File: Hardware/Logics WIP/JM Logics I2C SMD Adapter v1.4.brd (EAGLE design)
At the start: 52.4 x 31.2 mm, 30 parts, among them IC1 MEGA328P, J2 2.1MMJACK, X1 16.00MHz

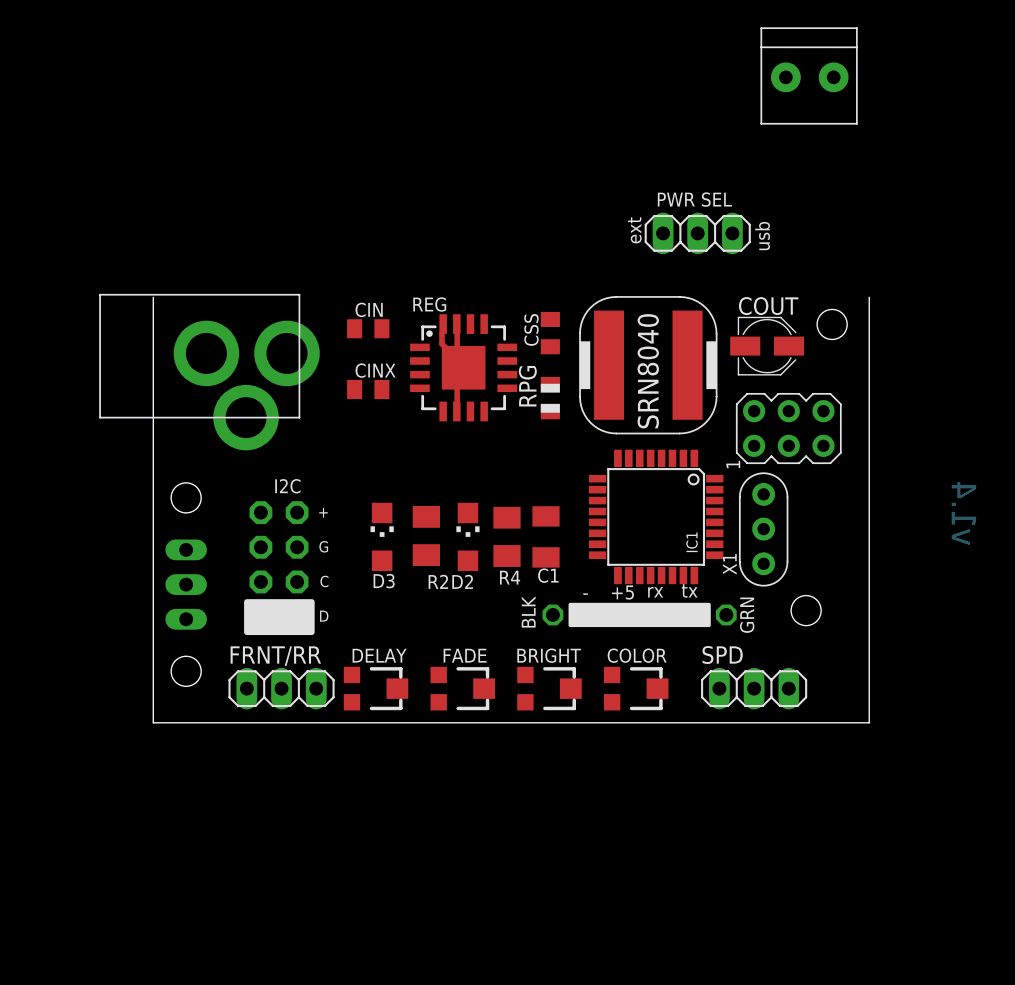
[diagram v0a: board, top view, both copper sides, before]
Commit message: 
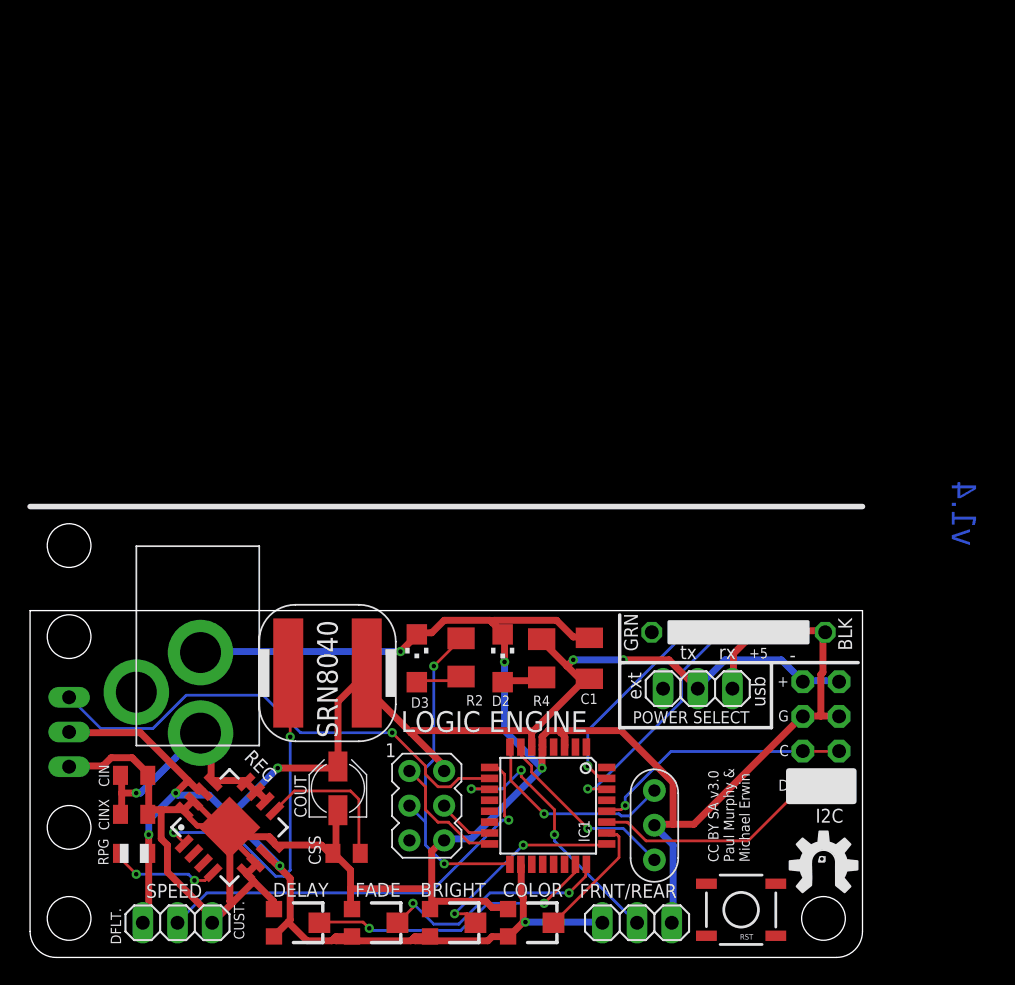
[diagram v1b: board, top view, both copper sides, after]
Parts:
- removed 5VIN: 1X2-3.5MM, adafruit:1X2-3.5MM
- removed FRNT/RR, SPD: (no value), pinhead:1X03
- added FRNT/REAR, SPEED: (no value), pinhead:1X03
- added RST: (no value), SparkFun-Electromechanical:TACTILE_SWITCH_SMD
- X1: value 16.00MHz -> 16MHz
- moved U$2 66.2 mm to (58.0, 6.79), flipped to the top
- moved U$1 59.4 mm to (73.5, 15.2)
- moved RPG 45.2 mm to (7.62, 7.62), turned to 180 degrees
- moved COUT 45.1 mm to (22.5, 12.4), turned to 90 degrees
- moved I2C 41.6 mm to (56.6, 16.4)
- moved I2C1 41.6 mm to (59.2, 16.4)
- moved CSS 40.9 mm to (23.2, 7.62), turned to 180 degrees
- moved ICSP 38.3 mm to (29.1, 11.1), turned to 0 degrees
- moved REG 37.8 mm to (14.6, 9.53), turned to 45 degrees
- moved CIN 36.9 mm to (7.62, 13.3)
- moved CINX 35.5 mm to (7.62, 10.5)
- moved PWR_SEL1 33.3 mm to (48.9, 19.7)
- moved INDUCTOR 32.6 mm to (17.8, 16.8)
- moved X1 23.1 mm to (45.7, 9.68)
- moved IC1 22.6 mm to (37.9, 11.1)
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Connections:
- net +5V: now also FRNT/REAR.1, SPEED.1; no longer FRNT/RR.1, SPD.1
- net DIGITAL5: now also SPEED.2; no longer SPD.2
- net DIGITAL7: now also FRNT/REAR.2; no longer FRNT/RR.2
- net GND: now also FRNT/REAR.3, SPEED.3; no longer FRNT/RR.3, SPD.3
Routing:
- net GND: track 0.00 -> 175.9 mm, vias 0 -> 3
- net +5V: track 0.00 -> 142.6 mm, vias 0 -> 7
- net DIGITAL6: track 0.00 -> 36.1 mm, vias 0 -> 1
- net DIGITAL5: track 0.00 -> 32.2 mm, vias 0 -> 1
- net N$3: track 0.00 -> 25.7 mm, vias 0 -> 2
- net SCK: track 0.00 -> 24.7 mm, vias 0 -> 2
- net ANALOG0: track 0.00 -> 21.3 mm, vias 0 -> 2
- net DIGITAL7: track 0.00 -> 20.3 mm, vias 0 -> 3
- net ANALOG4: track 0.00 -> 19.3 mm
- net ANALOG5: track 0.00 -> 19.2 mm, vias 0 -> 1
- net N$6: track 0.00 -> 19.1 mm, vias 0 -> 1
- net ANALOG1: track 0.00 -> 17.5 mm, vias 0 -> 2
- net RXD: track 0.00 -> 17.2 mm, vias 0 -> 1
- net ANALOG2: track 0.00 -> 15.1 mm, vias 0 -> 2
- net N$2: track 0.00 -> 14.9 mm, vias 0 -> 1
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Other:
- board size 52.4 x 31.2 mm -> 61 x 25.4 mm
- board text added: "CC BY SA v3.0 Paul Murphy & Michael Erwin"
- board text added: "CUST."
- board text added: "DFLT."
- board text added: "LOGIC ENGINE"
- board text added: "POWER SELECT"
- board text removed: "Logic Engine CC v3 BY SA 2013 Paul Murphy & Michael Erwin"
- board text removed: "PWR SEL"
- board text removed: "X1"

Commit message: Need to repackage inductor on Logic Engine to include GND (duh!)
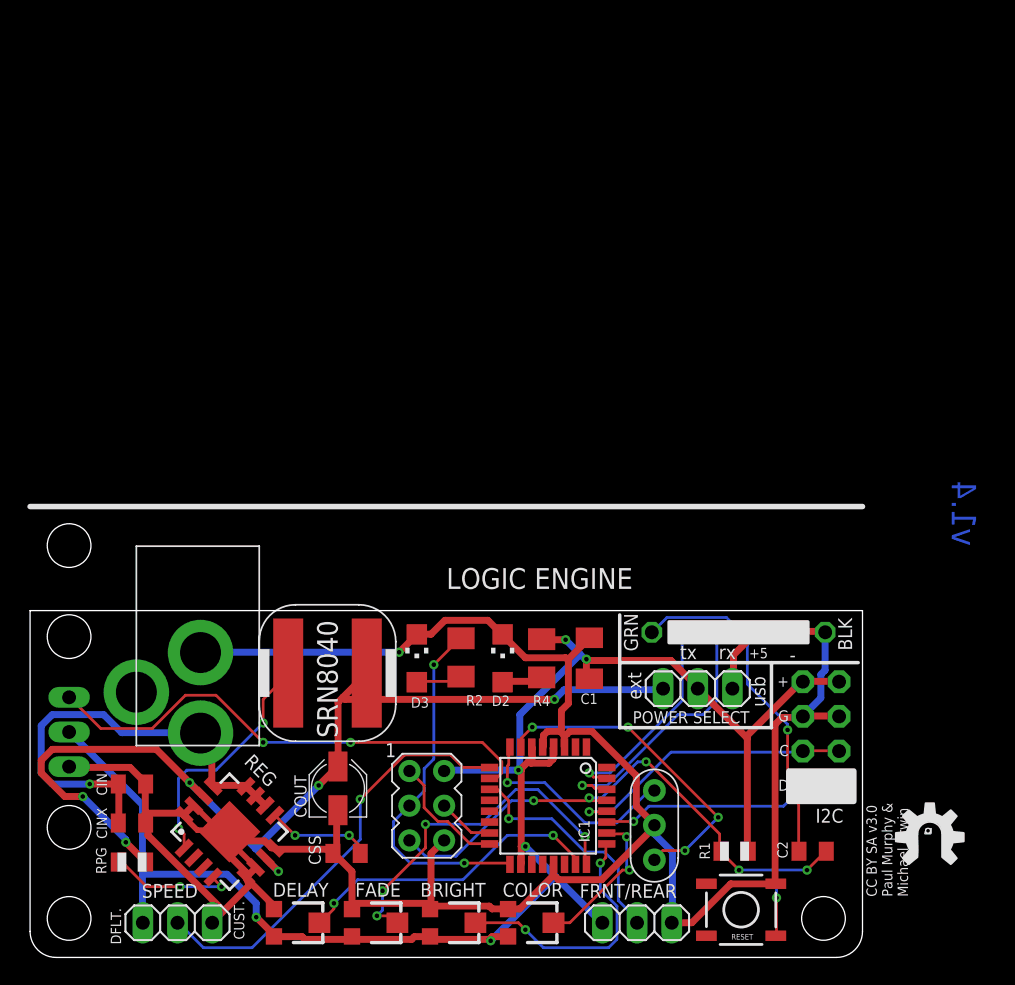
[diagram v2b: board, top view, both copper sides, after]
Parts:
- added C2: 0.1uF, adafruit:C0805K
- added R1: 10k, adafruit:R0805
- moved U$2 8.05 mm to (65.8, 8.86)
- moved CIN 0.65 mm to (7.46, 12.7)
- moved CINX 0.65 mm to (7.46, 9.84)
- moved RPG 0.65 mm to (7.46, 6.99)
- moved REG 0.32 mm to (14.6, 9.21)
- renumbered RST to RESET
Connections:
- net +5V: now also R1.2; no longer COUT.+, INDUCTOR.P$2, REG.14, REG.7, RPG.1
- net GND: now also RESET.3
- net N$9: now also COUT.+, INDUCTOR.P$2, REG.14, REG.7, RPG.1
- net RST: now also C2.2, IC1.29, R1.1, RESET.1
- net RTS#: now also C2.1
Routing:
- net N$9: track 0.00 -> 75.7 mm, vias 0 -> 6
- net RST: track 0.00 -> 44.7 mm, vias 0 -> 6
- net RTS#: track 0.00 -> 25.2 mm, vias 0 -> 1
- net +5V: track 142.6 -> 125.6 mm, vias 7 -> 6
- net N$6: track 19.1 -> 33.7 mm
- net N$1: track 13.8 -> 24.2 mm, vias 1 -> 4
- net ANALOG1: track 17.5 -> 26.1 mm, vias 2 -> 4
- net N$3: track 25.7 -> 17.6 mm
- net ANALOG2: track 15.1 -> 19.1 mm
- net N$7: track 11.1 -> 7.76 mm, vias 0 -> 2
- net DIGITAL7: track 20.3 -> 17.3 mm, vias 3 -> 1
- net ANALOG5: track 19.2 -> 21.5 mm
- net RXD: track 17.2 -> 19.5 mm
- net GND: track 175.9 -> 178.0 mm, vias 3 -> 1
- net ANALOG3: track 9.30 -> 11.3 mm, vias 0 -> 2
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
